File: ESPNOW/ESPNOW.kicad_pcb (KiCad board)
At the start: 4 copper layers, 40.4 x 120.4 mm, 56 parts, among them J1 USB_C_Receptacle_USB2.0_16P, J10 Conn_01x03_Pin, J11 Conn_01x03_Pin, J12 Conn_01x03_Pin, J13 Conn_01x03_Pin, J14 Screw_Terminal_01x02, J2 Screw_Terminal_01x14, J3 Conn_01x03_Pin, J4 Screw_Terminal_01x02, J5 Screw_Terminal_01x02, J6 Conn_01x03_Pin, J7 Conn_01x03_Pin, J8 Conn_01x03_Pin, J9 Conn_01x03_Pin, SW1 RESET, U1 ESP32-S3-WROOM-1, U2 DRV8848, U4 TPS564255

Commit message: Third Iteration
Reduced board length

TODO: Shift terminal left
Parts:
- moved D4 25.3 mm to (251.9, 44.8)
- moved C3 24.6 mm to (228.9, 123.9), turned to -90 degrees
- moved C2 24.6 mm to (226.5, 123.9), turned to -90 degrees
- moved R7 20.6 mm to (252.0, 48.9), turned to 90 degrees
- moved R2 14.9 mm to (243.3, 135.6), turned to 90 degrees
- moved R1 13.1 mm to (228.3, 136.8), turned to 180 degrees
- moved J5 10.9 mm to (238.8, 143.4), turned to 0 degrees
- moved C12 10.4 mm to (227.1, 133.3)
- moved C13 10.4 mm to (229.6, 133.3)
- moved R4 10.4 mm to (227.1, 128.6)
- moved R6 10.4 mm to (229.6, 128.6)
- moved REF** 10.0 mm to (250.0, 144.4)
- moved REF** 10.0 mm to (219.6, 144.4)
- moved R17 8.93 mm to (231.3, 123.8)
- moved C14 7.72 mm to (231.3, 119.2)
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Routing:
- net /IO9: track 2.85 -> 19.7 mm, vias 0 -> 2
- net /DRV8848/AOUT2: track 15.9 -> 6.23 mm, vias 1 -> 0
- net /IO10: track 86.8 -> 78.5 mm
- net /IO38: track 102.3 -> 94.5 mm
- net +3V3: track 183.2 -> 175.6 mm
- net Net-(U2-BISEN): track 3.27 -> 10.6 mm, vias 0 -> 2
- net /IO39: track 103.9 -> 96.7 mm
- net /IO21: track 99.6 -> 92.5 mm
- net /IO40: track 104.6 -> 97.5 mm
- net /DRV8848/BOUT1: track 17.2 -> 10.2 mm, vias 1 -> 0
- net /IO42: track 103.8 -> 97.3 mm
- net /IO41: track 101.8 -> 95.4 mm
- net /DRV8848/AOUT1: track 14.6 -> 8.91 mm, vias 1 -> 0
- net /DRV8848/BOUT2: track 17.4 -> 13.1 mm, vias 1 -> 0
- net Net-(U2-AISEN): track 3.04 -> 6.87 mm, vias 0 -> 2
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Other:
- board size 40.4 x 120.4 mm -> 40.4 x 110.4 mm

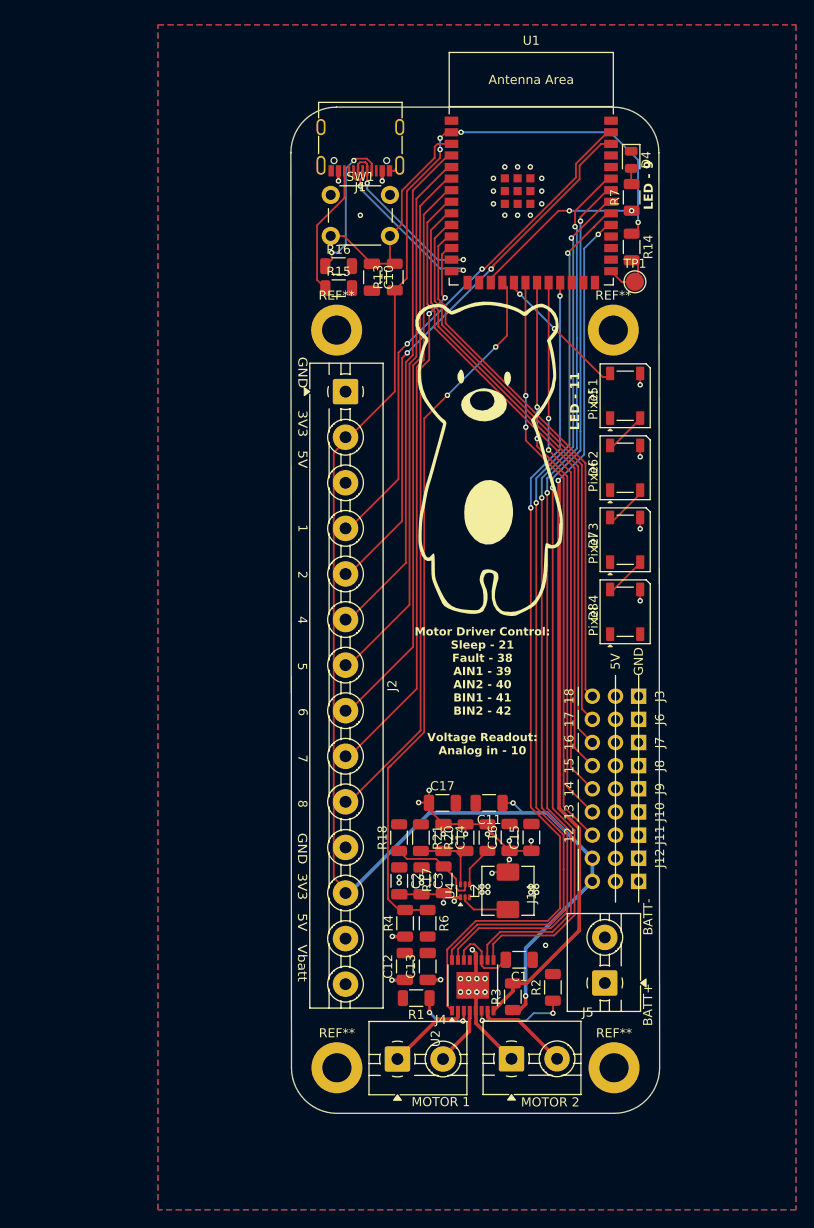
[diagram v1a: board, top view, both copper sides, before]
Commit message: Third Iteration
Reworked general layout to reduce size

Reworked Motor Driver routing to comply with layout guidelines in datasheet

Reworked Buck Converter routing to comply with layout guidelines in datasheet

TODO:
Add info to back layer
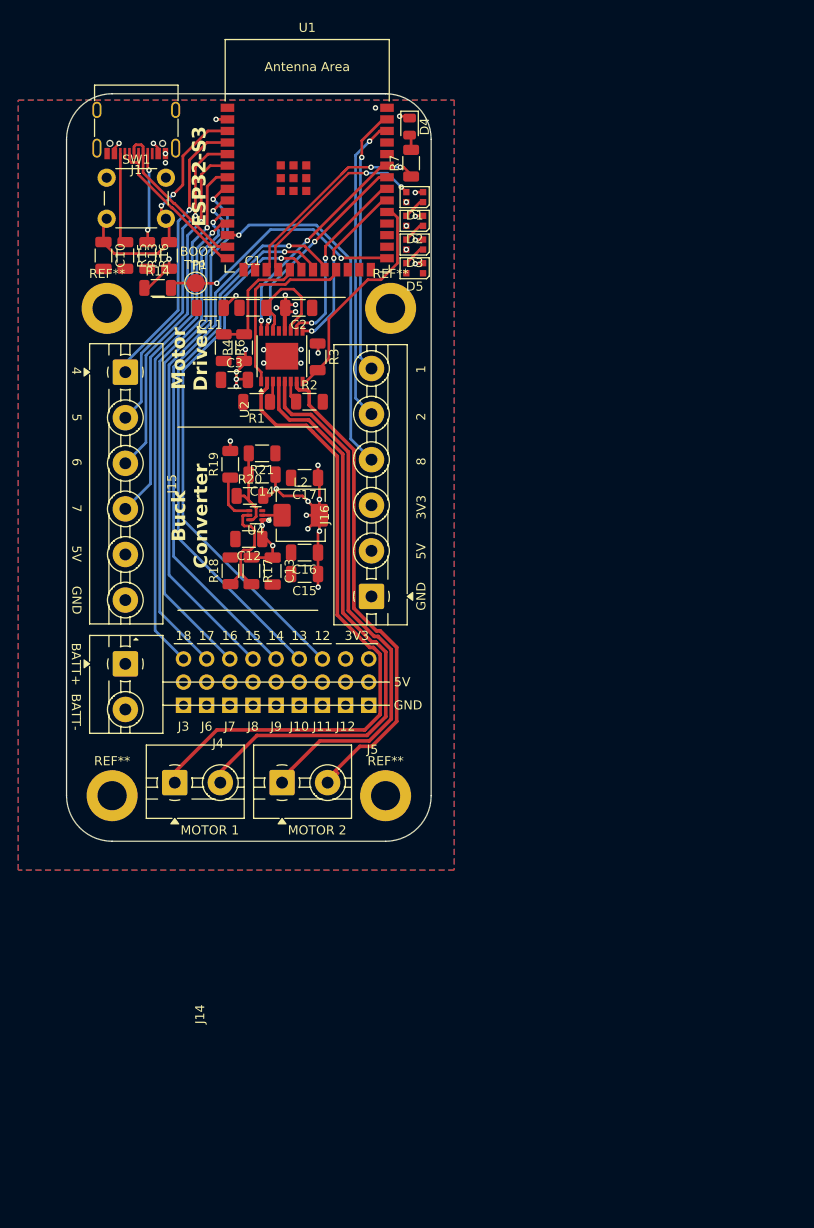
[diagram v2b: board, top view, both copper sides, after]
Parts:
- removed D6, D7, D8: WS2812B, LED_SMD:LED_WS2812B_PLCC4_5.0x5.0mm_P3.2mm
- removed G***: LOGO, footprints:Bear_40
- removed J2: Screw_Terminal_01x14, TerminalBlock:TerminalBlock_MaiXu_MX126-5.0-14P_1x14_P5.00mm
- added D1: WS2812B-2020, LED_SMD:LED_WS2812B-2020_PLCC4_2.0x2.0mm, F.Cu at (228.2, 48.9)
- added D2: WS2812B-2020, LED_SMD:LED_WS2812B-2020_PLCC4_2.0x2.0mm, F.Cu at (228.2, 51.5)
- added D3: WS2812B-2020, LED_SMD:LED_WS2812B-2020_PLCC4_2.0x2.0mm, F.Cu at (228.2, 54.1)
- added J15: Screw_Terminal_01x06, TerminalBlock:TerminalBlock_MaiXu_MX126-5.0-06P_1x06_P5.00mm, F.Cu at (196.4, 68.1)
- added J16: Screw_Terminal_01x06, TerminalBlock:TerminalBlock_MaiXu_MX126-5.0-06P_1x06_P5.00mm, F.Cu at (223.4, 92.7)
- D5: value WS2812B -> WS2812B-2020; footprint LED_SMD:LED_WS2812B_PLCC4_5.0x5.0mm_P3.2mm -> LED_SMD:LED_WS2812B-2020_PLCC4_2.0x2.0mm
- R1, R2: value R -> 500m
- moved C1 77.3 mm to (210.4, 61.1), turned to 0 degrees
- moved R3 73.4 mm to (217.5, 66.4), turned to -90 degrees
- moved U2 72.1 mm to (213.6, 66.4)
- moved R2 69.6 mm to (216.6, 71.4), turned to 0 degrees
- moved R1 67.7 mm to (210.8, 71.4)
- moved R6 67.0 mm to (207.2, 65.4)
- moved R4 65.6 mm to (209.4, 65.4)
- moved C2 63.8 mm to (215.4, 61.1), turned to 180 degrees
- moved J14 63.2 mm to (196.4, 100.1), turned to -90 degrees
- moved C11 62.3 mm to (205.7, 61.1)
- moved C3 58.7 mm to (208.4, 69.0), turned to 0 degrees
- moved R14 52.2 mm to (200.0, 58.9), turned to 0 degrees
- moved J3 49.9 mm to (202.8, 104.7), turned to 180 degrees
- moved C12 49.9 mm to (210.0, 86.4), turned to 180 degrees
- moved R19 49.7 mm to (207.9, 78.2)
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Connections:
- D5 pad 1: GND -> unconnected-(D5-DOUT-Pad1)
- D5 pad 2: Net-(D5-DOUT) -> +5V
- D5 pad 3: +5V -> Net-(D3-DOUT)
- D5 pad 4: /IO11 -> GND
- R4 pad 2: /IO10 -> /IO11
- R6 pad 1: /IO10 -> /IO11
- U2 pad 10: /IO42 -> /IO40
- U2 pad 15: /IO40 -> /IO41
- U2 pad 16: /IO39 -> /IO42
- U2 pad 9: /IO41 -> /IO39
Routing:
- net /IO39: track 96.7 -> 18.9 mm
- net /IO40: track 97.5 -> 21.2 mm
- net +3V3: track 175.6 -> 99.4 mm, vias 6 -> 4
- net /IO42: track 97.3 -> 24.0 mm
- net /IO41: track 95.4 -> 22.8 mm
- net /IO21: track 92.5 -> 20.4 mm, vias 2 -> 0
- net /IO38: track 94.5 -> 24.8 mm, vias 2 -> 0
- net /DRV8848/AOUT1: track 8.91 -> 69.8 mm
- net /DRV8848/AOUT2: track 6.23 -> 64.0 mm
- net /IO10: track 78.5 -> 21.2 mm
- net /DRV8848/BOUT2: track 13.1 -> 57.9 mm
- net /DRV8848/BOUT1: track 10.2 -> 52.5 mm
- net /IO8: track 65.9 -> 38.4 mm, vias 2 -> 1
- net /IO1: track 55.7 -> 29.3 mm, vias 2 -> 1
- net /IO2: track 59.7 -> 33.7 mm, vias 2 -> 1
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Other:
- board size 40.4 x 110.4 mm -> 40 x 82 mm
- board text added: "3V3"
- board text added: "BATT+ BATT-"
- board text added: "BOOT TP"
- board text added: "Buck Converter"
- board text added: "ESP32-S3"
- board text added: "Motor Driver"
- board text removed: "BATT+"
- board text removed: "BATT-"
- board text removed: "GND 3V3 5V"
- board text removed: "GND 3V3 5V Vbatt"
- board text removed: "LED - 11"
- board text removed: "LED - 9"
- board text removed: "Motor Driver Control: Sleep - 21 Fault - 38 AIN1 - 39 AIN2 - 40 BIN1 - 41 BIN2 - 42 Voltage Readout: Analog in - 10"
- board text removed: "Pixel 1"
- board text removed: "Pixel 2"
- board text removed: "Pixel 3"
- board text removed: "Pixel 4"
